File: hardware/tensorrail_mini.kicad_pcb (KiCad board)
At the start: 2 copper layers, 80 x 50 mm, 59 parts, among them J1 USB_C_PWR, J2 JTAG, J3 EXPANSION, J4 FEATHER_L, J5 FEATHER_R, SW1 RESET, SW2 BOOT, U1 TPS62130_3V3, U2 TPS62130_1V2, U3 INA219, U4 W25Q128, U5 50MHz

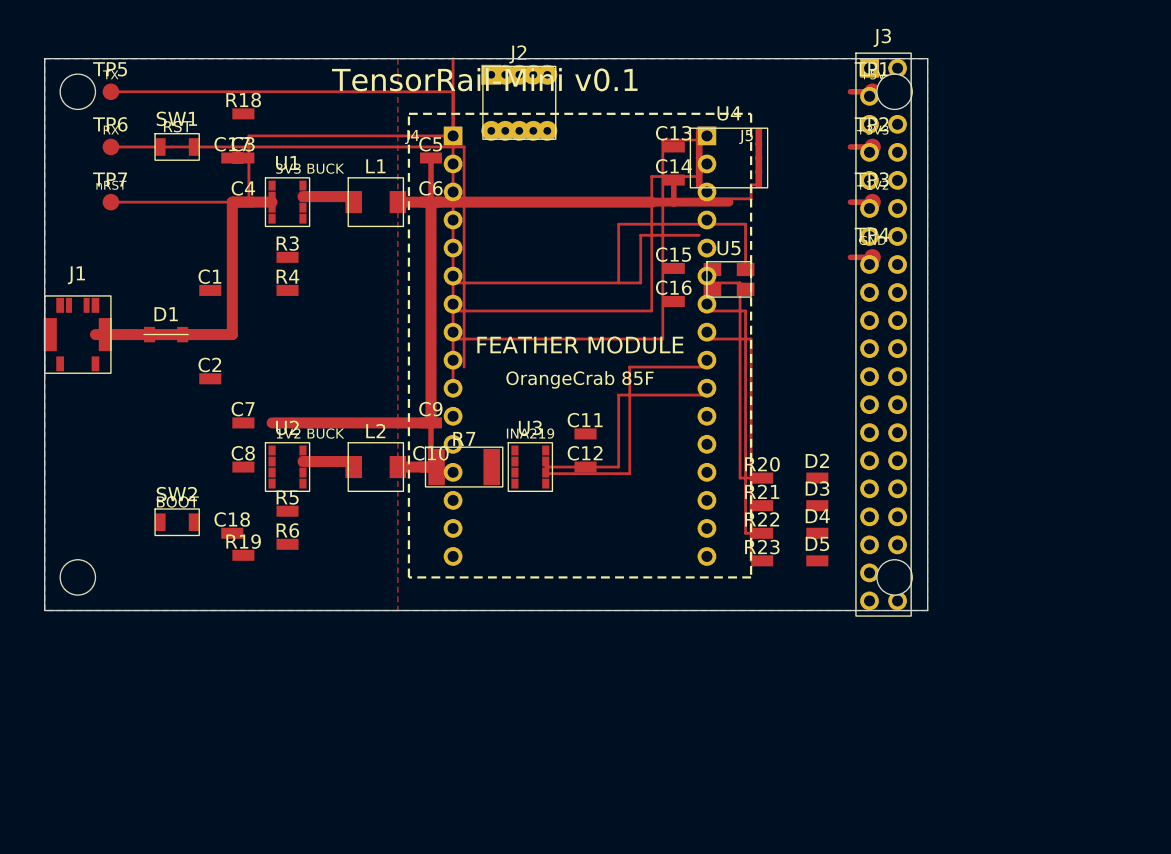
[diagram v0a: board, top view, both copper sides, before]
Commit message: Replace viewer design artifacts with clean layouts
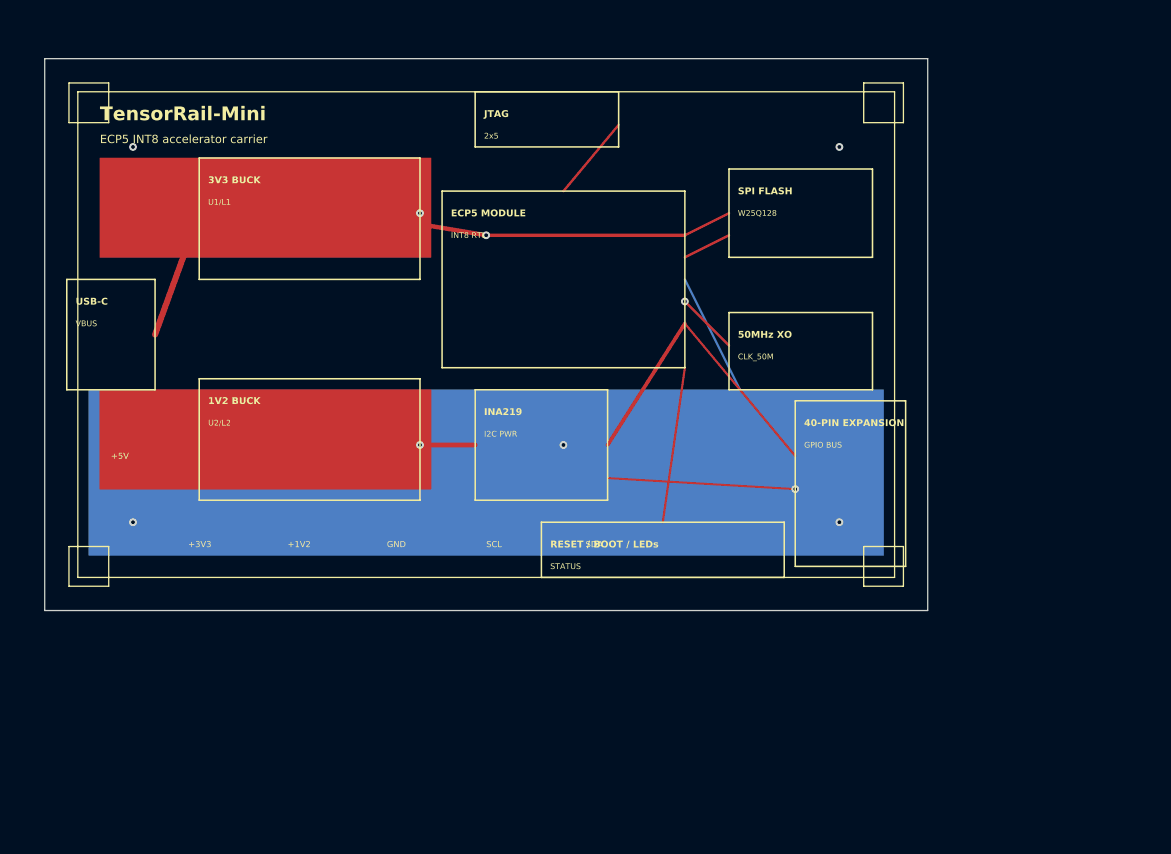
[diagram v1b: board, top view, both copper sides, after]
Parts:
- removed C1, C10, C11, C13, C15, C17, C18, C2, C4, C6, C8: 100nF, Capacitor_SMD:C_0402_1005Metric
- removed C12, C14, C16: 10nF, Capacitor_SMD:C_0402_1005Metric
- removed C3, C7: 10uF, Capacitor_SMD:C_0402_1005Metric
- removed C5, C9: 100uF, Capacitor_SMD:C_0402_1005Metric
- removed D1: B5819W, Diode_SMD:D_SOD-123
- removed D2: LED_PWR, LED_SMD:LED_0402_1005Metric
- removed D3: LED_BUSY, LED_SMD:LED_0402_1005Metric
- removed D4: LED_DONE, LED_SMD:LED_0402_1005Metric
- removed D5: LED_HB, LED_SMD:LED_0402_1005Metric
- removed J1: USB_C_PWR, Connector_USB:USB_C_Receptacle_USB2.0_GCT_USB4135-GF-A_Vertical
- removed J2: JTAG, Connector_IDC:IDC_Header_2x05_P1.27mm_Vertical
- removed J3: EXPANSION, Connector_PinHeader_2.54mm:PinHeader_2x20_P2.54mm_Vertical
- removed J4: FEATHER_L, Connector_PinSocket_2.54mm:PinSocket_1x16_P2.54mm_Vertical
- removed J5: FEATHER_R, Connector_PinSocket_2.54mm:PinSocket_1x16_P2.54mm_Vertical
- removed L1: 2.2uH, Inductor_SMD:L_4040
- removed L2: 1.5uH, Inductor_SMD:L_4040
- removed MH1, MH2, MH3, MH4: M3, MountingHole:MountingHole_3.2mm_M3
- removed R18, R19: 10k, Resistor_SMD:R_0402_1005Metric
- removed R20, R21, R22, R23: 330R, Resistor_SMD:R_0402_1005Metric
- removed R3: 464k, Resistor_SMD:R_0402_1005Metric
- removed R4, R6: 100k, Resistor_SMD:R_0402_1005Metric
- removed R5: 103k, Resistor_SMD:R_0402_1005Metric
- removed R7: 0R1, Resistor_SMD:R_2512_6332Metric
- removed SW1: RESET, Button_Switch_SMD:SW_SPST_B3U-1000P
- removed SW2: BOOT, Button_Switch_SMD:SW_SPST_B3U-1000P
- removed TP1: +5V, TestPoint:TestPoint_SMD_Pad_D1.5mm
- removed TP2: +3V3, TestPoint:TestPoint_SMD_Pad_D1.5mm
- removed TP3: +1V2, TestPoint:TestPoint_SMD_Pad_D1.5mm
- removed TP4: GND, TestPoint:TestPoint_SMD_Pad_D1.5mm
- removed TP5: UART_TX, TestPoint:TestPoint_SMD_Pad_D1.5mm
- removed TP6: UART_RX, TestPoint:TestPoint_SMD_Pad_D1.5mm
- removed TP7: RESET_N, TestPoint:TestPoint_SMD_Pad_D1.5mm
- removed U1: TPS62130_3V3, Package_TO_SOT_SMD:SOT-23-8
- removed U2: TPS62130_1V2, Package_TO_SOT_SMD:SOT-23-8
- removed U3: INA219, Package_TO_SOT_SMD:SOT-23-8
- removed U4: W25Q128, Package_SO:SOIC-8_3.9x4.9mm_P1.27mm
- removed U5: 50MHz, Oscillator:Oscillator_SMD_Epson_SG-8002CA-4Pin_3.2x2.5mm
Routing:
- net (no net): track 0.00 -> 165.4 mm, vias 0 -> 10
- net +3V3: track 72.4 -> 0.00 mm
- net UART_TX: track 58.5 -> 0.00 mm
- net UART_RX: track 51.9 -> 0.00 mm
- net RESET_N: track 44.0 -> 0.00 mm
- net SPI_MISO: track 40.3 -> 0.00 mm
- net SPI_MOSI: track 34.5 -> 0.00 mm
- net SPI_SCK: track 26.6 -> 0.00 mm
- net LED_DONE: track 24.6 -> 0.00 mm
- net LED_HB: track 24.6 -> 0.00 mm
- net SDA: track 24.3 -> 0.00 mm
- net LED_BUSY: track 22.2 -> 0.00 mm
- net SCL: track 21.1 -> 0.00 mm
- net CLK_50M: track 20.9 -> 0.00 mm
- net VBUS_RAW: track 20.1 -> 0.00 mm
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- removed copper zone on B.Cu, net GND
- removed copper zone on F.Cu, net GND
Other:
- board text added: "2x5"
- board text added: "40-PIN EXPANSION"
- board text added: "50MHz XO"
- board text added: "CLK_50M"
- board text added: "ECP5 INT8 accelerator carrier"
- board text added: "ECP5 MODULE"
- board text added: "GPIO BUS"
- board text added: "I2C PWR"
- board text added: "INT8 RTL"
- board text added: "JTAG"
- board text added: "RESET / BOOT / LEDs"
- board text added: "SCL"
- board text added: "SDA"
- board text added: "SPI FLASH"
- board text added: "STATUS"
- board text added: "TensorRail-Mini"
- board text added: "U1/L1"
- board text added: "U2/L2"
- board text added: "USB-C"
- board text added: "VBUS"
- board text added: "W25Q128"
- board text removed: "FEATHER MODULE"
- board text removed: "OrangeCrab 85F"
- board text removed: "RX"
- board text removed: "TX"
- board text removed: "TensorRail-Mini v0.1"
- board text removed: "nRST"

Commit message: Make KiCad viewer artifacts readable
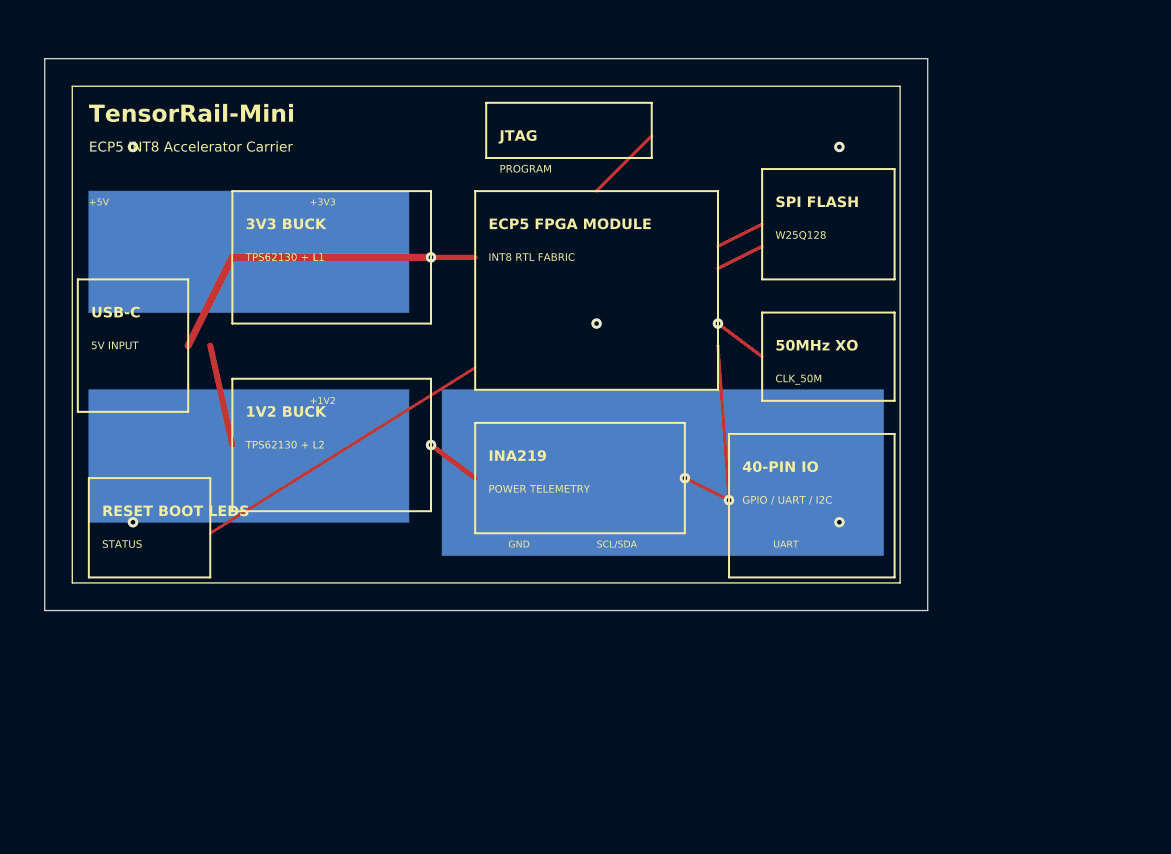
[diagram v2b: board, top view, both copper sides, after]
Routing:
- net (no net): track 165.4 -> 113.0 mm
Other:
- board text added: "40-PIN IO"
- board text added: "5V INPUT"
- board text added: "ECP5 FPGA MODULE"
- board text added: "ECP5 INT8 Accelerator Carrier"
- board text added: "GPIO / UART / I2C"
- board text added: "INT8 RTL FABRIC"
- board text added: "POWER TELEMETRY"
- board text added: "PROGRAM"
- board text added: "RESET BOOT LEDS"
- board text added: "SCL/SDA"
- board text added: "TPS62130 + L1"
- board text added: "TPS62130 + L2"
- board text added: "UART"
- board text removed: "2x5"
- board text removed: "40-PIN EXPANSION"
- board text removed: "ECP5 INT8 accelerator carrier"
- board text removed: "ECP5 MODULE"
- board text removed: "GPIO BUS"
- board text removed: "I2C PWR"
- board text removed: "INT8 RTL"
- board text removed: "RESET / BOOT / LEDs"
- board text removed: "SCL"
- board text removed: "SDA"
- board text removed: "U1/L1"
- board text removed: "U2/L2"
- board text removed: "VBUS"

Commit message: Rebuild TensorRail KiCad hardware artifacts
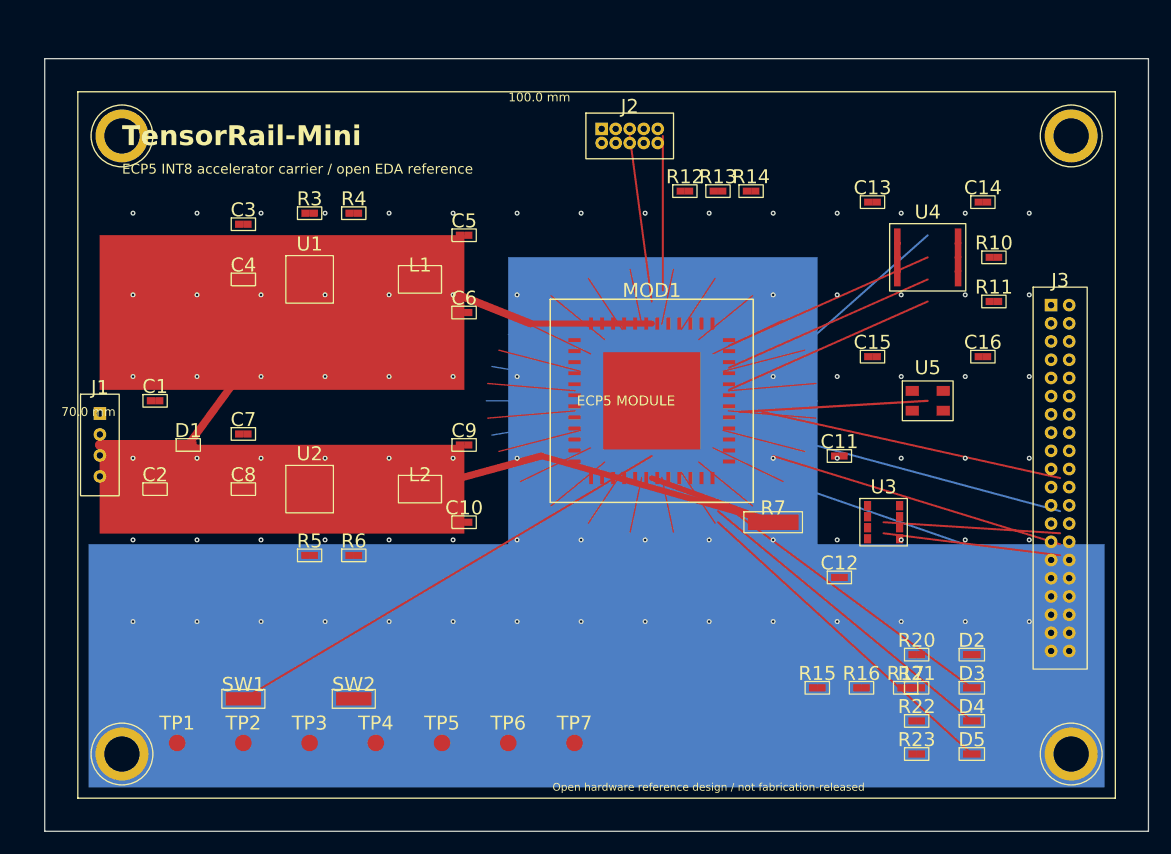
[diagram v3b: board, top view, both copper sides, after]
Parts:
- added C1: 100n, Discrete_SMD:C1, F.Cu at (10.0, 31.0)
- added C10: 100n, Discrete_SMD:C10, F.Cu at (38.0, 42.0)
- added C11: 100n, Discrete_SMD:C11, F.Cu at (72.0, 36.0)
- added C12: 10n, Discrete_SMD:C12, F.Cu at (72.0, 47.0)
- added C13: 100n, Discrete_SMD:C13, F.Cu at (75.0, 13.0)
- added C14: 10n, Discrete_SMD:C14, F.Cu at (85.0, 13.0)
- added C15: 100n, Discrete_SMD:C15, F.Cu at (75.0, 27.0)
- added C16: 10n, Discrete_SMD:C16, F.Cu at (85.0, 27.0)
- added C2: 100n, Discrete_SMD:C2, F.Cu at (10.0, 39.0)
- added C3: 10u, Discrete_SMD:C3, F.Cu at (18.0, 15.0)
- added C4: 100n, Discrete_SMD:C4, F.Cu at (18.0, 20.0)
- added C5: 100u, Discrete_SMD:C5, F.Cu at (38.0, 16.0)
- added C6: 100n, Discrete_SMD:C6, F.Cu at (38.0, 23.0)
- added C7: 10u, Discrete_SMD:C7, F.Cu at (18.0, 34.0)
- added C8: 100n, Discrete_SMD:C8, F.Cu at (18.0, 39.0)
- added C9: 100u, Discrete_SMD:C9, F.Cu at (38.0, 35.0)
- added D1: PMEG, Discrete_SMD:D1, F.Cu at (13.0, 35.0)
- added D2: LED, Discrete_SMD:D2, F.Cu at (84.0, 54.0)
- added D3: LED, Discrete_SMD:D3, F.Cu at (84.0, 57.0)
- added D4: LED, Discrete_SMD:D4, F.Cu at (84.0, 60.0)
- added D5: LED, Discrete_SMD:D5, F.Cu at (84.0, 63.0)
- added J1: USB-C_PWR, Connector_Generic:1x4_Header, F.Cu at (5.00, 35.0)
- added J2: JTAG, Connector_Generic:5x2_Header, F.Cu at (53.0, 7.00)
- added J3: EXPANSION, Connector_Generic:2x20_Header, F.Cu at (92.0, 38.0)
- added L1: 2.2uH, Discrete_SMD:L1, F.Cu at (34.0, 20.0)
- added L2: 1.5uH, Discrete_SMD:L2, F.Cu at (34.0, 39.0)
- added MH1: M3, MountingHole:MountingHole_3.2mm_M3, F.Cu at (7.00, 7.00)
- added MH2: M3, MountingHole:MountingHole_3.2mm_M3, F.Cu at (93.0, 7.00)
- added MH3: M3, MountingHole:MountingHole_3.2mm_M3, F.Cu at (7.00, 63.0)
- added MH4: M3, MountingHole:MountingHole_3.2mm_M3, F.Cu at (93.0, 63.0)
- added MOD1: OrangeCrab_85F, Module:ECP5_Feather_Module_Socket, F.Cu at (55.0, 31.0)
- added R10: 10k, Discrete_SMD:R10, F.Cu at (86.0, 18.0)
- added R11: 10k, Discrete_SMD:R11, F.Cu at (86.0, 22.0)
- added R12: 100R, Discrete_SMD:R12, F.Cu at (58.0, 12.0)
- added R13: 100R, Discrete_SMD:R13, F.Cu at (61.0, 12.0)
- added R14: 100R, Discrete_SMD:R14, F.Cu at (64.0, 12.0)
- added R15: 4k7, Discrete_SMD:R15, F.Cu at (70.0, 57.0)
- added R16: 4k7, Discrete_SMD:R16, F.Cu at (74.0, 57.0)
- added R17: 4k7, Discrete_SMD:R17, F.Cu at (78.0, 57.0)
- added R20: 330R, Discrete_SMD:R20, F.Cu at (79.0, 54.0)
- added R21: 330R, Discrete_SMD:R21, F.Cu at (79.0, 57.0)
- added R22: 330R, Discrete_SMD:R22, F.Cu at (79.0, 60.0)
- added R23: 330R, Discrete_SMD:R23, F.Cu at (79.0, 63.0)
- added R3: 464k, Discrete_SMD:R3, F.Cu at (24.0, 14.0)
- added R4: 100k, Discrete_SMD:R4, F.Cu at (28.0, 14.0)
- added R5: 103k, Discrete_SMD:R5, F.Cu at (24.0, 45.0)
- added R6: 100k, Discrete_SMD:R6, F.Cu at (28.0, 45.0)
- added R7: 0R1_SHUNT, Discrete_SMD:R7, F.Cu at (66.0, 42.0)
- added SW1: RESET, Discrete_SMD:SW1, F.Cu at (18.0, 58.0)
- added SW2: BOOT, Discrete_SMD:SW2, F.Cu at (28.0, 58.0)
- added TP1: +5V, TestPoint:TestPoint_Pad_D1.5mm, F.Cu at (12.0, 62.0)
- added TP2: +3V3, TestPoint:TestPoint_Pad_D1.5mm, F.Cu at (18.0, 62.0)
- added TP3: +1V2, TestPoint:TestPoint_Pad_D1.5mm, F.Cu at (24.0, 62.0)
- added TP4: GND, TestPoint:TestPoint_Pad_D1.5mm, F.Cu at (30.0, 62.0)
- added TP5: SCL, TestPoint:TestPoint_Pad_D1.5mm, F.Cu at (36.0, 62.0)
- added TP6: SDA, TestPoint:TestPoint_Pad_D1.5mm, F.Cu at (42.0, 62.0)
- added TP7: CLK_50M, TestPoint:TestPoint_Pad_D1.5mm, F.Cu at (48.0, 62.0)
- added U1: TPS62130_3V3, Package_TO_SOT_SMD:SOT-23-8, F.Cu at (24.0, 20.0)
- added U2: TPS62130_1V2, Package_TO_SOT_SMD:SOT-23-8, F.Cu at (24.0, 39.0)
- added U3: INA219, Package_TO_SOT_SMD:SOT-23-8, F.Cu at (76.0, 42.0)
- added U4: W25Q128, Package_SO:SOIC-8_3.9x4.9mm_P1.27mm, F.Cu at (80.0, 18.0)
- added U5: 50MHz, Oscillator:Oscillator_3.2x2.5, F.Cu at (80.0, 31.0)
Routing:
- net (no net): track 113.0 -> 0.00 mm, vias 10 -> 0
- net +3V3: track 0.00 -> 73.0 mm
- net +1V2: track 0.00 -> 72.8 mm
- net GPIO0: track 0.00 -> 67.2 mm
- net GPIO1: track 0.00 -> 66.5 mm
- net SPI_SCK: track 0.00 -> 59.2 mm
- net SPI_MISO: track 0.00 -> 59.2 mm
- net SPI_MOSI: track 0.00 -> 59.2 mm
- net RESET_N: track 0.00 -> 43.0 mm
- net GND: track 0.00 -> 39.6 mm, vias 0 -> 81
- net BOOT_N: track 0.00 -> 35.0 mm
- net LED_HB: track 0.00 -> 31.1 mm
- net LED_DONE: track 0.00 -> 29.8 mm
- net LED_BUSY: track 0.00 -> 28.6 mm
- net UART_RX: track 0.00 -> 27.5 mm
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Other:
- board size 80 x 50 mm -> 100 x 70 mm
- board text added: "100.0 mm"
- board text added: "70.0 mm"
- board text added: "ECP5 INT8 accelerator carrier / open EDA reference"
- board text added: "Open hardware reference design / not fabrication-released"
- board text removed: "+1V2"
- board text removed: "+3V3"
- board text removed: "+5V"
- board text removed: "1V2 BUCK"
- board text removed: "3V3 BUCK"
- board text removed: "40-PIN IO"
- board text removed: "50MHz XO"
- board text removed: "5V INPUT"
- board text removed: "CLK_50M"
- board text removed: "ECP5 FPGA MODULE"
- board text removed: "ECP5 INT8 Accelerator Carrier"
- board text removed: "GND"
- board text removed: "GPIO / UART / I2C"
- board text removed: "INA219"
- board text removed: "INT8 RTL FABRIC"
- board text removed: "JTAG"
- board text removed: "POWER TELEMETRY"
- board text removed: "PROGRAM"
- board text removed: "RESET BOOT LEDS"
- board text removed: "SCL/SDA"
- board text removed: "SPI FLASH"
- board text removed: "STATUS"
- board text removed: "TPS62130 + L1"
- board text removed: "TPS62130 + L2"
- board text removed: "UART"
- board text removed: "USB-C"
- board text removed: "W25Q128"
